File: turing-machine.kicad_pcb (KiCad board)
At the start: 2 copper layers, 11 parts, among them J1 Conn_02x05_Odd_Even

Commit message: PCB layout complete
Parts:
- added C10: 0.47u, Capacitor_THT:C_Rect_L7.2mm_W2.5mm_P5.00mm_FKS2_FKP2_MKS2_MKP2, B.Cu at (71.4, 80.9)
- added C11: 1n, Capacitor_SMD:C_0805_2012Metric, F.Cu at (65.3, 77.1)
- added C12: 0.47u, Capacitor_THT:C_Rect_L7.2mm_W2.5mm_P5.00mm_FKS2_FKP2_MKS2_MKP2, B.Cu at (71.4, 68.2)
- added C13: 100n, Capacitor_SMD:C_0805_2012Metric, F.Cu at (94.4, 44.5)
- added C14: 100n, Capacitor_SMD:C_0805_2012Metric, F.Cu at (97.8, 41.1)
- added C15: 100n, Capacitor_SMD:C_0805_2012Metric, F.Cu at (93.9, 59.7)
- added C16: 1n, Capacitor_SMD:C_0805_2012Metric, F.Cu at (54.4, 59.9)
- added C17: 1n, Capacitor_SMD:C_0805_2012Metric, F.Cu at (65.0, 62.0)
- added C18: 1n, Capacitor_SMD:C_0805_2012Metric, F.Cu at (76.5, 57.4)
- added C19: 100n, Capacitor_SMD:C_0805_2012Metric, F.Cu at (59.6, 62.0)
- added C20: 100n, Capacitor_SMD:C_0805_2012Metric, F.Cu at (72.4, 55.1)
- added C21: 100n, Capacitor_SMD:C_0805_2012Metric, F.Cu at (82.4, 33.5)
- added C22: 100n, Capacitor_SMD:C_0805_2012Metric, F.Cu at (80.0, 44.2)
- added C23: 100n, Capacitor_SMD:C_0805_2012Metric, F.Cu at (73.6, 24.9)
- added C24: 100n, Capacitor_SMD:C_0805_2012Metric, F.Cu at (71.5, 35.8)
- added C25: 100n, Capacitor_SMD:C_0805_2012Metric, F.Cu at (71.0, 84.1)
- added C3: 330p, Capacitor_SMD:C_0805_2012Metric, F.Cu at (59.5, 67.4)
- added C4: 100n, Capacitor_SMD:C_0805_2012Metric, F.Cu at (84.6, 74.3)
- added C5: 100n, Capacitor_SMD:C_0805_2012Metric, F.Cu at (82.5, 70.3)
- added C6: 100n, Capacitor_SMD:C_0805_2012Metric, F.Cu at (76.2, 16.3)
- added C7: 10n, Capacitor_SMD:C_0805_2012Metric, F.Cu at (72.6, 16.3)
- added C8: 1n, Capacitor_SMD:C_0805_2012Metric, F.Cu at (83.8, 82.0)
- added C9: 0.47u, Capacitor_THT:C_Rect_L7.2mm_W2.5mm_P5.00mm_FKS2_FKP2_MKS2_MKP2, B.Cu at (66.1, 92.0)
- added D10: LED_GREEN, LED_THT:LED_D3.0mm, F.Cu at (59.0, -5.04)
- added D11: LED_GREEN, LED_THT:LED_D3.0mm, F.Cu at (52.7, -5.04)
- added D12: LED_GREEN, LED_THT:LED_D3.0mm, F.Cu at (53.0, 71.9)
- added D13: LED_GREEN, LED_THT:LED_D3.0mm, F.Cu at (90.6, 71.9)
- added D3: 1N4148, Diode_SMD:D_SOD-323_HandSoldering, F.Cu at (84.9, 70.0)
- added D4: LED_GREEN, LED_THT:LED_D3.0mm, F.Cu at (97.2, -5.04)
- added D5: LED_GREEN, LED_THT:LED_D3.0mm, F.Cu at (90.8, -5.04)
- added D6: LED_GREEN, LED_THT:LED_D3.0mm, F.Cu at (84.5, -5.04)
- added D7: LED_GREEN, LED_THT:LED_D3.0mm, F.Cu at (78.1, -5.04)
- added D8: LED_GREEN, LED_THT:LED_D3.0mm, F.Cu at (71.8, -5.04)
- added D9: LED_GREEN, LED_THT:LED_D3.0mm, F.Cu at (65.4, -5.04)
- added H10: noise, Eurorack:Mech-AudioJack-Hole-Output, F.Cu at (82.8, 214.8)
- added H11: b0, Eurorack:Mech-LED-Hole-3mm, F.Cu at (66.7, 116.8)
- added H12: b1, Eurorack:Mech-LED-Hole-3mm, F.Cu at (73.0, 116.8)
- added H13: b2, Eurorack:Mech-LED-Hole-3mm, F.Cu at (79.4, 116.8)
- added H14: b3, Eurorack:Mech-LED-Hole-3mm, F.Cu at (85.7, 116.8)
- added H15: b4, Eurorack:Mech-LED-Hole-3mm, F.Cu at (92.1, 116.8)
- added H16: b5, Eurorack:Mech-LED-Hole-3mm, F.Cu at (98.4, 116.8)
- added H17: b6, Eurorack:Mech-LED-Hole-3mm, F.Cu at (60.3, 116.8)
- added H18: b7, Eurorack:Mech-LED-Hole-3mm, F.Cu at (54.0, 116.8)
- added H19: clk_led, Eurorack:Mech-LED-Hole-3mm, F.Cu at (54.3, 193.6)
- added H20: length, Eurorack:Mech-MRK-Hole, F.Cu at (62.2, 164.0)
- added H21: write, Eurorack:Mech-2M_Switch-Hole, F.Cu at (94.0, 159.3)
- added H22: pulse, Eurorack:Mech-AudioJack-Hole-Output-Gate, F.Cu at (94.9, 201.3)
- added H23: pulse_led, Eurorack:Mech-LED-Hole-3mm, F.Cu at (91.9, 193.6)
- added H5: cv, Eurorack:Mech-AudioJack-Hole-Input-CV, F.Cu at (57.4, 214.8)
- added H6: change, Eurorack:Mech-Potentiometer-Hole_level_180deg, F.Cu at (76.2, 136.1)
- added H7: clock, Eurorack:Mech-AudioJack-Hole-Input-Clock, F.Cu at (57.3, 201.3)
- added H8: scale, Eurorack:Mech-Potentiometer-Hole_level, F.Cu at (81.5, 191.6)
- added H9: out, Eurorack:Mech-AudioJack-Hole-Output-CV, F.Cu at (95.0, 214.8)
- added J2: cv, Eurorack:AudioJack2_Tayda_A-2566, F.Cu at (57.4, 93.0)
- added J3: clock, Eurorack:AudioJack2_Tayda_A-2566, F.Cu at (57.3, 79.5)
- added J4: out, Eurorack:AudioJack2_Tayda_A-2566, F.Cu at (95.0, 93.0)
- added J5: noise, Eurorack:AudioJack2_Tayda_A-2566, F.Cu at (82.8, 93.0)
- added J6: GATES, Eurorack:PinHeader_2x08_P2.54mm_Vertical, B.Cu at (94.6, 25.4)
- added J7: PULSES, Eurorack:PinHeader_2x08_P2.54mm_Vertical, B.Cu at (83.8, 25.4)
- added J8: pulse, Eurorack:AudioJack2_Tayda_A-2566, F.Cu at (94.9, 79.5)
- added Q1: BC547, Package_TO_SOT_THT:TO-92_Inline_Wide, B.Cu at (70.9, 96.4)
- added R10: 15K, Resistor_SMD:R_0805_2012Metric, F.Cu at (80.3, 70.3)
- added R11: 15K, Resistor_SMD:R_0805_2012Metric, F.Cu at (84.6, 78.1)
- added R12: 10K, Resistor_SMD:R_0805_2012Metric, F.Cu at (83.5, 66.8)
- added R13: 5.1K, Resistor_SMD:R_0805_2012Metric, F.Cu at (81.5, 82.0)
- added R14: 3.3K, Resistor_SMD:R_0805_2012Metric, F.Cu at (69.1, 3.85)
- added R15: 1.6K, Resistor_SMD:R_0805_2012Metric, F.Cu at (69.1, 6.80)
- added R16: 1.6K, Resistor_SMD:R_0805_2012Metric, F.Cu at (69.3, 9.75)
- added R17: 100K, Resistor_SMD:R_0805_2012Metric, F.Cu at (65.8, 88.9)
- added R18: 10K, Resistor_SMD:R_0805_2012Metric, F.Cu at (70.4, 88.9)
- added R19: 470K, Resistor_SMD:R_0805_2012Metric, F.Cu at (68.1, 88.9)
- added R20: 1K, Resistor_SMD:R_0805_2012Metric, F.Cu at (67.6, 77.1)
- added R21: 100K, Resistor_SMD:R_0805_2012Metric, F.Cu at (70.4, 70.0)
- added R22: 1K, Resistor_SMD:R_0805_2012Metric, F.Cu at (70.6, 77.9)
- added R23: 2.2K, Resistor_SMD:R_0805_2012Metric, F.Cu at (53.5, 66.5)
- added R24: 1K, Resistor_SMD:R_0805_2012Metric, F.Cu at (97.8, 37.3)
- added R25: 10K, Resistor_SMD:R_0805_2012Metric, F.Cu at (99.2, 49.5)
- added R26: 10K, Resistor_SMD:R_0805_2012Metric, F.Cu at (88.5, 47.5)
- added R27: 10K, Resistor_SMD:R_0805_2012Metric, F.Cu at (88.5, 51.3)
- added R28: 47K, Resistor_SMD:R_0805_2012Metric, F.Cu at (88.5, 55.1)
- added R29: 100K, Resistor_SMD:R_0805_2012Metric, F.Cu at (99.2, 53.9)
- added R3: 10K, Resistor_SMD:R_0805_2012Metric, F.Cu at (85.8, -1.74)
- added R30: 10K, Resistor_SMD:R_0805_2012Metric, F.Cu at (54.3, 56.3)
- added R31: 10K, Resistor_SMD:R_0805_2012Metric, F.Cu at (65.0, 58.3)
- added R32: 10K, Resistor_SMD:R_0805_2012Metric, F.Cu at (76.5, 61.2)
- added R33: 2.2K, Resistor_SMD:R_0805_2012Metric, F.Cu at (96.5, 70.8)
- added R4: 10K, Resistor_SMD:R_0805_2012Metric, F.Cu at (66.7, -1.74)
- added R5: 100K, Resistor_SMD:R_0805_2012Metric, F.Cu at (76.2, 1.31)
- added R6: 51K, Resistor_SMD:R_0805_2012Metric, F.Cu at (88.5, 58.9)
- added R7: 15K, Resistor_SMD:R_0805_2012Metric, F.Cu at (59.4, 72.1)
- added R8: 100K, Resistor_SMD:R_0805_2012Metric, F.Cu at (59.5, 69.7)
- added R9: 470K, Resistor_SMD:R_0805_2012Metric, F.Cu at (78.0, 70.3)
- added RN1: 2.2K, Resistor_THT:R_Array_SIP9, B.Cu at (98.1, -9.10)
- added RV1: B50K, Eurorack:Potentiometer_RV16AF-41-15R1, F.Cu at (76.2, 14.3)
- added RV2: B50K, Eurorack:Potentiometer_RV16AF-41-15R1, F.Cu at (81.5, 69.8)
- added RV3: 1M, Potentiometer_THT:Potentiometer_Bourns_3296W_Vertical, B.Cu at (67.1, 74.0)
- added SW1: SW_Rotary12, Eurorack:Switch_Rotary_NKK_MRK_112, F.Cu at (62.2, 42.2)
- added SW2: SW_SPDT_MSM, Eurorack:Switch_SPDT_Tayda_A-5751, F.Cu at (94.0, 37.5)
- added U1: TL072, Package_SO:SOIC-8_3.9x4.9mm_P1.27mm, F.Cu at (80.5, 76.2)
- added U10: 4050, Package_SO:TSSOP-16_4.4x5mm_P0.65mm, F.Cu at (78.6, 40.4)
- added U11: L78L09_SOT89, Package_TO_SOT_SMD:SOT-89-3, F.Cu at (79.9, 48.6)
- added U12: 4081, Package_SO:TSSOP-14_4.4x5mm_P0.65mm, F.Cu at (77.8, 24.8)
- added U13: 4081, Package_SO:TSSOP-14_4.4x5mm_P0.65mm, F.Cu at (71.2, 32.0)
- added U14: TL072, Package_SO:SOIC-8_3.9x4.9mm_P1.27mm, F.Cu at (66.9, 83.0)
- added U2: DAC08, Package_SO:SOIC-16_3.9x9.9mm_P1.27mm, F.Cu at (75.6, 8.68)
- added U3: TL431DBZ, Package_TO_SOT_SMD:SOT-23, F.Cu at (69.1, 13.5)
- added U4: 4016, Package_SO:TSSOP-14_4.4x5mm_P0.65mm, F.Cu at (93.9, 48.5)
- added U5: TL072, Package_SO:SOIC-8_3.9x4.9mm_P1.27mm, F.Cu at (93.9, 55.6)
- added U6: 4015, Package_SO:TSSOP-16_4.4x5mm_P0.65mm, F.Cu at (59.8, 58.0)
- added U7: 4015, Package_SO:TSSOP-16_4.4x5mm_P0.65mm, F.Cu at (71.1, 59.2)
- added U8: L78L09_SOT89, Package_TO_SOT_SMD:SOT-89-3, F.Cu at (78.0, 34.1)
- added U9: 4050, Package_SO:TSSOP-16_4.4x5mm_P0.65mm, F.Cu at (86.5, 34.8)
- D1, D2, R1, R2: moved to F.Cu
- moved H4 205.4 mm to (96.5, 227.1)
- moved H3 202.0 mm to (56.0, 227.1)
- moved H2 102.2 mm to (96.5, 104.6)
- moved H1 89.6 mm to (56.0, 104.6)
- moved C1 60.8 mm to (65.2, 2.58), turned to 180 degrees
- moved C2 54.6 mm to (62.7, 17.8), turned to 0 degrees
- moved J1 49.2 mm to (57.4, 5.12)
- moved D2 48.9 mm to (62.2, 14.5)
- moved R1 48.2 mm to (61.3, 11.2)
- moved R2 48.1 mm to (61.3, 8.93)
- moved D1 47.9 mm to (62.2, 5.63)
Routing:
- net +12V: track 14.0 -> 328.9 mm, vias 0 -> 10
- net GND: track 0.00 -> 250.8 mm, vias 0 -> 23
- net -12V: track 15.8 -> 221.2 mm, vias 0 -> 5
- net /B6': track 0.00 -> 158.0 mm, vias 0 -> 3
- net /B5': track 0.00 -> 151.7 mm, vias 0 -> 3
- net /B0': track 0.00 -> 149.6 mm, vias 0 -> 3
- net /B1': track 0.00 -> 147.7 mm, vias 0 -> 3
- net /B2': track 0.00 -> 146.7 mm, vias 0 -> 3
- net /B4': track 0.00 -> 143.7 mm, vias 0 -> 4
- net /B3': track 0.00 -> 140.9 mm, vias 0 -> 3
- net /B7': track 0.00 -> 139.2 mm, vias 0 -> 4
- net Net-(U1B--): track 0.00 -> 99.5 mm, vias 0 -> 2
- net /CLK': track 0.00 -> 94.6 mm, vias 0 -> 3
- net /_CLK2': track 0.00 -> 89.3 mm
- net /_CLK': track 0.00 -> 73.4 mm, vias 0 -> 4
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- added copper zone on B.Cu, net /FACE
- added copper zone on F.Cu, net /FACE
- added copper zone on B.Cu, net GND
- added copper zone on F.Cu, net GND
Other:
- board outline added: 50.5 x 241 mm
- board text added: "11"
- board text added: "12"
- board text added: "13"
- board text added: "16"
- board text added: "2"
- board text added: "3"
- board text added: "4"
- board text added: "5"
- board text added: "6"
- board text added: "7"
- board text added: "8"
- board text added: "9"
- board text added: "BITS->VOLTS"
- board text added: "Based on the Music Thing Modular design github.com/TomWhitwell/TuringMachine"
- board text added: "EXPANSIONS"
- board text added: "GATES"
- board text added: "INPUT OUTPUT"
- board text added: "LOOP CTRL"
- board text added: "NOISE"
- board text added: "PULSES"
- board text added: "SHIFT REGISTERS"
- board text added: "thismatters/turing-machine/v0"
- board text added: "turing machine"

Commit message: fix: getting all parts sorted out
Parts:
- C10, C12, C9: value 0.47u -> 470n box
- J6: value GATES -> Conn_02x08_Odd_Even
- J7: value PULSES -> Conn_02x08_Odd_Even
- SW2: footprint Eurorack:Switch_SPDT_Tayda_A-5751 -> Eurorack:Switch_SPDT_1M_Solder_Lug
- moved SW2 12.4 mm to (106.3, 38.7)
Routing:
- net /SOL': track 55.0 -> 44.6 mm
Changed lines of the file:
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@@
   (footprint "Eurorack:Switch_Rotary_NKK_MRK_112" (layer "F.Cu")
     (at 62.23 42.205)
+    (property "PartNum" "633-MRK112-BA")
     (property "Sheetfile" "turing-machine.kicad_sch")
     (property "Sheetname" "")
+    (property "Vendor" "Mouser")
     (property "ki_description" "rotary switch with 12 positions")
     (property "ki_keywords" "rotary switch")
@@
     )
   )
-  (footprint "Eurorack:Switch_SPDT_Tayda_A-5751" (layer "F.Cu")
-    (at 93.98 37.506)
+  (footprint "Eurorack:Switch_SPDT_1M_Solder_Lug" (layer "F.Cu")
+    (at 106.2998 38.685)
+    (property "PartNum" "A-6099")
     (property "Sheetfile" "turing-machine.kicad_sch")
     (property "Sheetname" "")
+    (property "Vendor" "Tayda")
     (property "ki_description" "Switch, single pole double throw, center OFF position")
     (property "ki_keywords" "switch spdt single-pole double-throw ON-OFF-ON")
     (attr through_hole)
-    (fp_text reference "SW2" (at 0.0508 5.207 unlocked) (layer "F.SilkS")
+    (fp_text reference "SW2" (at -1.5 -7 unlocked) (layer "F.SilkS")
+        (effects (font (size 1 1) (thickness 0.1)))
+    )
+    (fp_text value "SW_SPDT_MSM" (at 0 1 unlocked) (layer "F.Fab")
         (effects (font (size 1 1) (thickness 0.15)))
     )
-    (fp_text value "SW_SPDT_MSM" (at 0 5.08 unlocked) (layer "F.Fab")
+    (fp_text user "${REFERENCE}" (at 0 2.5 unlocked) (layer "F.Fab")
         (effects (font (size 1 1) (thickness 0.15)))
     )
-    (fp_rect (start -2.54 -4.065) (end 2.54 4.065)
-      (stroke (width 0.15) (type solid)) (fill none) (layer "F.SilkS"))
-    (fp_rect (start -2.8702 -4.2672) (end 2.8194 4.2672)
-      (stroke (width 0.12) (type solid)) (fill none) (layer "F.CrtYd"))
-    (pad "1" thru_hole circle (at 0 -2.54) (size 1.9 1.9) (drill 1) (layers "*.Cu" "*.Mask")
+    (fp_rect (start -3.43 -6.35) (end 3.43 6.35)
+      (stroke (width 0.1) (type default)) (fill none) (layer "F.SilkS"))
+    (fp_rect (start -3.55 -6.45) (end 3.55 6.5)
+      (stroke (width 0.05) (type default)) (fill none) (layer "F.CrtYd"))
+    (pad "1" thru_hole oval (at 0 -4.7) (size 3.3 2) (drill oval 2.5 1.3) (layers "*.Cu" "*.Mask")
       (net 1 "+12V") (pinfunction "1") (pintype "passive"))
-    (pad "2" thru_hole circle (at 0 0) (size 1.9 1.9) (drill 1) (layers "*.Cu" "*.Mask")
+    (pad "2" thru_hole oval (at 0.05 0.05) (size 3.3 2) (drill oval 2.5 1.3) (layers "*.Cu" "*.Mask")
       (net 82 "Net-(R24-Pad2)") (pinfunction "2") (pintype "passive"))
-    (pad "3" thru_hole circle (at 0 2.54) (size 1.9 1.9) (drill 1) (layers "*.Cu" "*.Mask")
+    (pad "3" thru_hole oval (at 0 4.7) (size 3.3 2) (drill oval 2.5 1.3) (layers "*.Cu" "*.Mask")
       (net 2 "GND") (pinfunction "3") (pintype "passive"))
   )
@@
         (effects (font (size 1 1) (thickness 0.15)) (justify mirror))
     )
-    (fp_text value "0.47u" (at 2.5 -2.5 90) (layer "B.Fab")
+    (fp_text value "470n box" (at 2.5 -2.5 90) (layer "B.Fab")
         (effects (font (size 1 1) (thickness 0.15)) (justify mirror))
     )
@@
     (descr "Through hole straight pin header, 2x08, 2.54mm pitch, double rows")
     (tags "Through hole pin header THT 2x08 2.54mm double row")
+    (property "PartNum" "A-2956")
     (property "Sheetfile" "turing-machine.kicad_sch")
     (property "Sheetname" "")
+    (property "Vendor" "Tayda")
     (property "ki_description" "Generic connector, double row, 02x08, odd/even pin numbering scheme (row 1 odd numbers, row 2 even numbers), script generated (kicad-library-utils/schlib/autogen/connector/)")
     (property "ki_keywords" "connector")
@@
         (effects (font (size 1 1) (thickness 0.15)) (justify mirror))
     )
-    (fp_text value "GATES" (at 0.0078 5.9372) (layer "B.Fab")
+    (fp_text value "Conn_02x08_Odd_Even" (at 0.0078 5.9372) (layer "B.Fab")
         (effects (font (size 1 1) (thickness 0.15)) (justify mirror))
     )
@@
         (effects (font (size 1 1) (thickness 0.15)) (justify mirror))
     )
-    (fp_text value "0.47u" (at 2.5 -2.5 90) (layer "B.Fab")
+    (fp_text value "470n box" (at 2.5 -2.5 90) (layer "B.Fab")
         (effects (font (size 1 1) (thickness 0.15)) (justify mirror))
     )
@@
     (descr "Through hole straight pin header, 2x08, 2.54mm pitch, double rows")
     (tags "Through hole pin header THT 2x08 2.54mm double row")
+    (property "PartNum" "A-2956")
     (property "Sheetfile" "turing-machine.kicad_sch")
     (property "Sheetname" "")
+    (property "Vendor" "Tayda")
     (property "ki_description" "Generic connector, double row, 02x08, odd/even pin numbering scheme (row 1 odd numbers, row 2 even numbers), script generated (kicad-library-utils/schlib/autogen/connector/)")
     (property "ki_keywords" "connector")
@@
         (effects (font (size 1 1) (thickness 0.15)) (justify mirror))
     )
-    (fp_text value "PULSES" (at 0.0008 5.9372) (layer "B.Fab")
+    (fp_text value "Conn_02x08_Odd_Even" (at 0.0008 5.9372) (layer "B.Fab")
         (effects (font (size 1 1) (thickness 0.15)) (justify mirror))
     )
@@
         (effects (font (size 1 1) (thickness 0.15)) (justify mirror))
     )
-    (fp_text value "0.47u" (at 2.5 -2.5) (layer "B.Fab")
+    (fp_text value "470n box" (at 2.5 -2.5) (layer "B.Fab")
         (effects (font (size 1 1) (thickness 0.15)) (justify mirror))
     )
@@
   (segment (start 96.4315 44.0156) (end 98.248404 44.0156) (width 0.25) (layer "F.Cu") (net 20))
   (segment (start 98.84 41.162) (end 97.79 40.112) (width 0.25) (layer "F.Cu") (net 20))
-  (segment (start 94.5114 44.9357) (end 94.5114 43.7455) (width 0.25) (layer "F.Cu") (net 20))
-  (segment (start 95.7639 43.348) (end 96.4315 44.0156) (width 0.25) (layer "F.Cu") (net 20))
-  (segment (start 94.5114 43.7455) (end 94.9089 43.348) (width 0.25) (layer "F.Cu") (net 20))
   (segment (start 87.356108 51.097637) (end 87.405937 51.097637) (width 0.25) (layer "F.Cu") (net 20))
   (segment (start 62.7049 56.3788) (end 63.442399 56.3788) (width 0.25) (layer "F.Cu") (net 20))
@@
   (segment (start 97.79 40.112) (end 97.79 38.1899) (width 0.25) (layer "F.Cu") (net 20))
   (segment (start 87.405937 51.097637) (end 88.5444 52.2361) (width 0.25) (layer "F.Cu") (net 20))
-  (segment (start 93.8425 45.6046) (end 94.5114 44.9357) (width 0.25) (layer "F.Cu") (net 20))
   (segment (start 98.248404 44.0156) (end 98.84 43.424004) (width 0.25) (layer "F.Cu") (net 20))
-  (segment (start 88.0083 45.6046) (end 93.8425 45.6046) (width 0.25) (layer "F.Cu") (net 20))
   (segment (start 63.442399 56.3788) (end 63.7674 56.053799) (width 0.25) (layer "F.Cu") (net 20))
   (segment (start 63.7674 54.2566) (end 64.389 53.635) (width 0.25) (layer "F.Cu") (net 20))
@@
   (segment (start 87.0694 49.698) (end 87.0694 46.5435) (width 0.25) (layer "F.Cu") (net 20))
   (segment (start 63.7674 56.053799) (end 63.7674 54.2566) (width 0.25) (layer "F.Cu") (net 20))
-  (segment (start 94.9089 43.348) (end 95.7639 43.348) (width 0.25) (layer "F.Cu") (net 20))
   (via (at 64.389 53.635) (size 0.8) (drill 0.4) (layers "F.Cu" "B.Cu") (net 20))
   (via (at 87.356108 51.097637) (size 0.8) (drill 0.4) (layers "F.Cu" "B.Cu") (net 20))

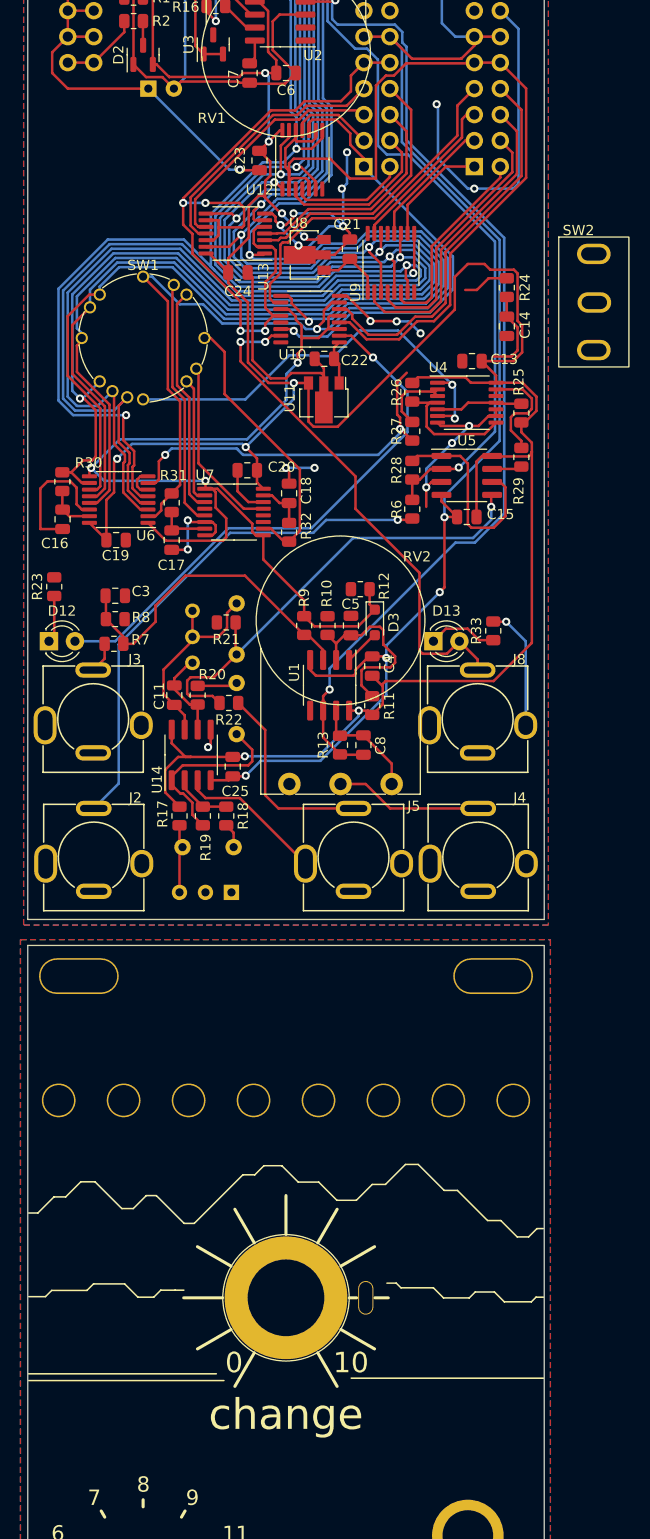
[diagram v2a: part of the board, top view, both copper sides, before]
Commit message: fix: available parts only
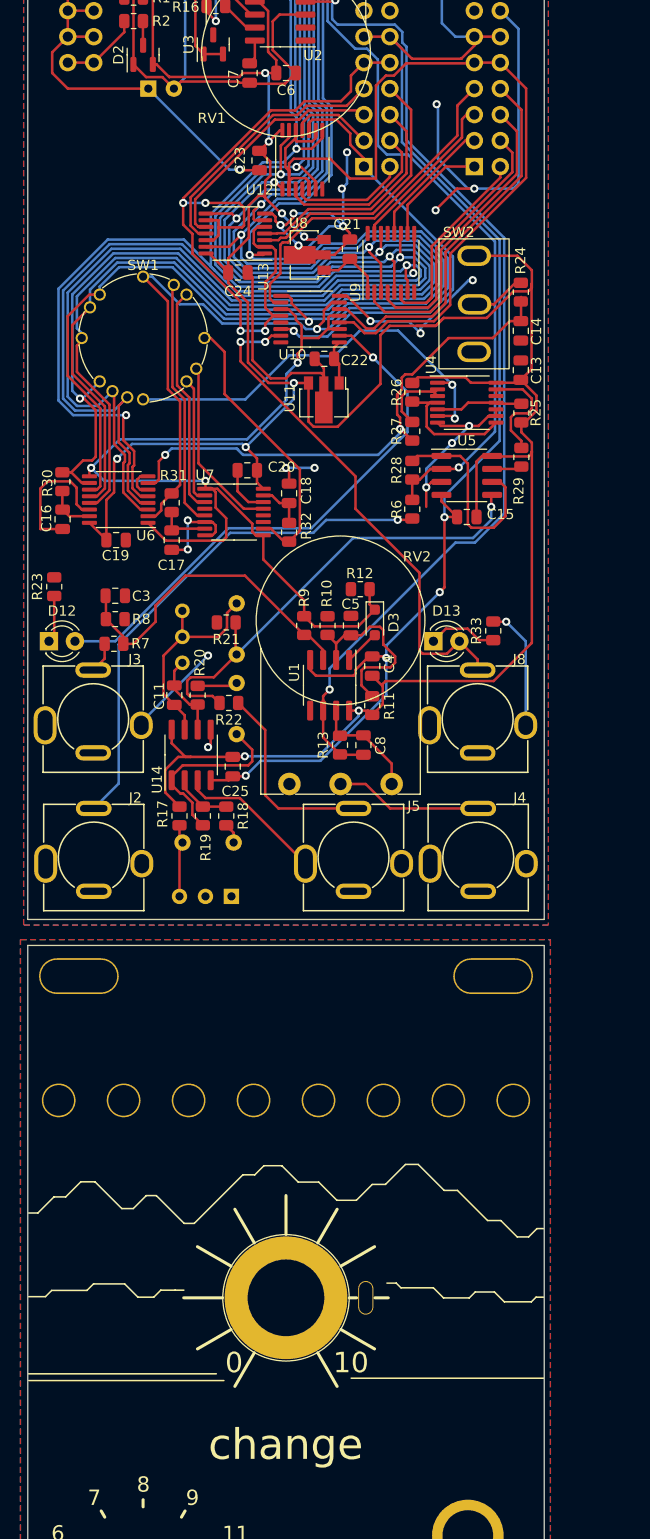
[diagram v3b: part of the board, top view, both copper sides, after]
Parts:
- C10, C12, C9: footprint Capacitor_THT:C_Rect_L7.2mm_W2.5mm_P5.00mm_FKS2_FKP2_MKS2_MKP2 -> Capacitor_THT:C_Rect_L7.2mm_W4.5mm_P5.00mm_FKS2_FKP2_MKS2_MKP2
- moved SW2 11.7 mm to (94.6, 38.9)
- moved C13 4.86 mm to (99.2, 45.3), turned to 90 degrees
- moved C14 1.44 mm to (99.2, 41.5)
- moved R24 1.44 mm to (99.2, 37.7)
- moved RV3 0.99 mm to (66.1, 74.0)
- moved C9 0.45 mm to (66.1, 91.5)
- moved Q1 0.39 mm to (70.9, 96.8)
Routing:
- net GND: track 250.8 -> 272.6 mm, vias 23 -> 25
- net /SOL': track 44.6 -> 51.9 mm
- net +12V: track 328.9 -> 336.0 mm
- net Net-(C11-Pad2): track 19.8 -> 20.8 mm
- net Net-(R24-Pad2): track 4.54 -> 5.39 mm
- net /G8: track 37.8 -> 37.1 mm

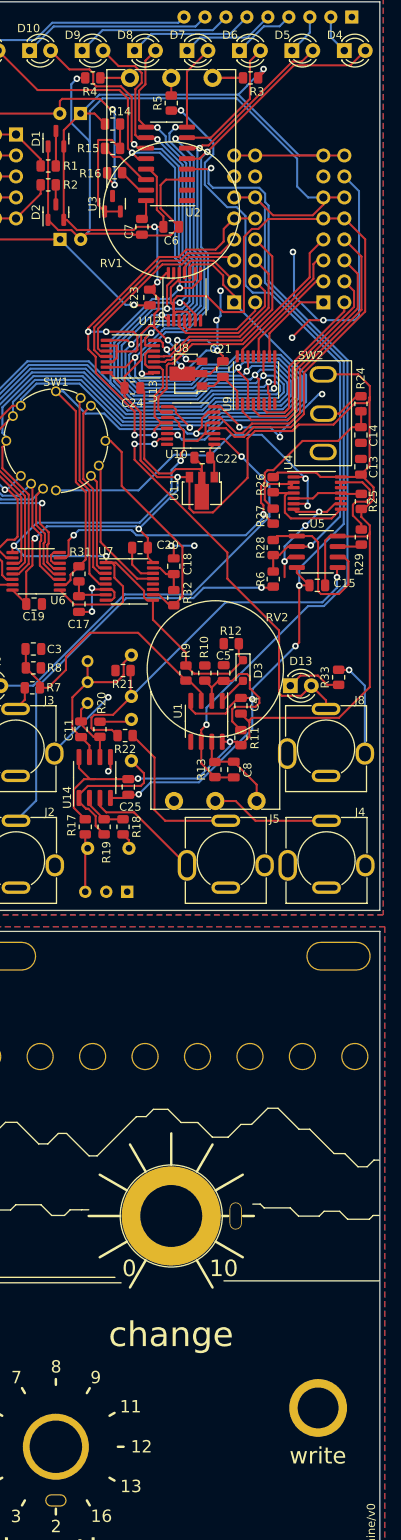
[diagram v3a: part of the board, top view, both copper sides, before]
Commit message: ready for v0 manu
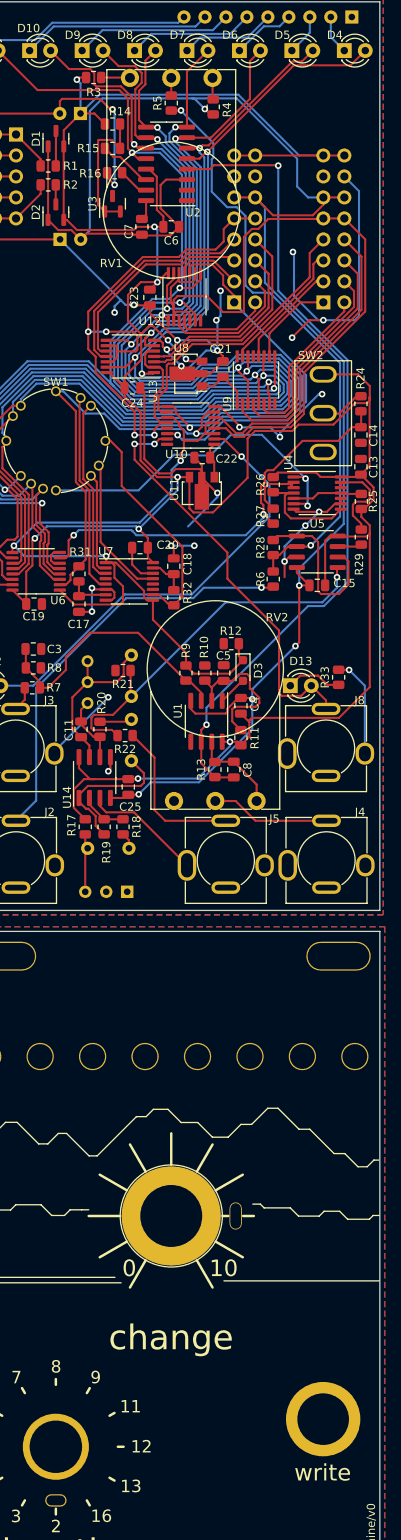
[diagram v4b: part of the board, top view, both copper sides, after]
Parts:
- H21: footprint Eurorack:Mech-2M_Switch-Hole -> Eurorack:Mech-1M_Switch-Hole
- R11: value 15K -> 68K
- RV3: value 1M -> 5K
- moved R3 19.0 mm to (66.8, -1.78), turned to 180 degrees
- moved R4 15.0 mm to (81.3, 1.78), turned to -90 degrees
- moved H21 1.49 mm to (94.6, 160.7)
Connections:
- RV1 pad 1: Net-(R3-Pad1) -> Net-(R4-Pad1)
- RV1 pad 3: Net-(R4-Pad1) -> Net-(R3-Pad1)
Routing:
- net GND: track 272.6 -> 287.9 mm, vias 25 -> 27
- net -12V: track 221.2 -> 213.8 mm
- net Net-(R3-Pad1): track 7.38 -> 3.44 mm
- net /_CLK': track 73.4 -> 74.6 mm
- net /P5: track 23.3 -> 24.4 mm
- net /P7: track 25.9 -> 27.1 mm
- net Net-(R4-Pad1): track 3.59 -> 2.52 mm
- net +12V: track 336.0 -> 336.9 mm
- net /LOOP_CTRL': track 73.1 -> 72.4 mm
- net Net-(U1B--): track 99.5 -> 100.2 mm
- net /B0': track 149.6 -> 149.0 mm
- net Net-(R24-Pad2): track 5.39 -> 4.87 mm
